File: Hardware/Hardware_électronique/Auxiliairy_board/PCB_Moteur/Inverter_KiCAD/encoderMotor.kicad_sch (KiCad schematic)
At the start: 3 parts, among them J3 Conn_02x05_Odd_Even, U1301 MAX3097ECSE+

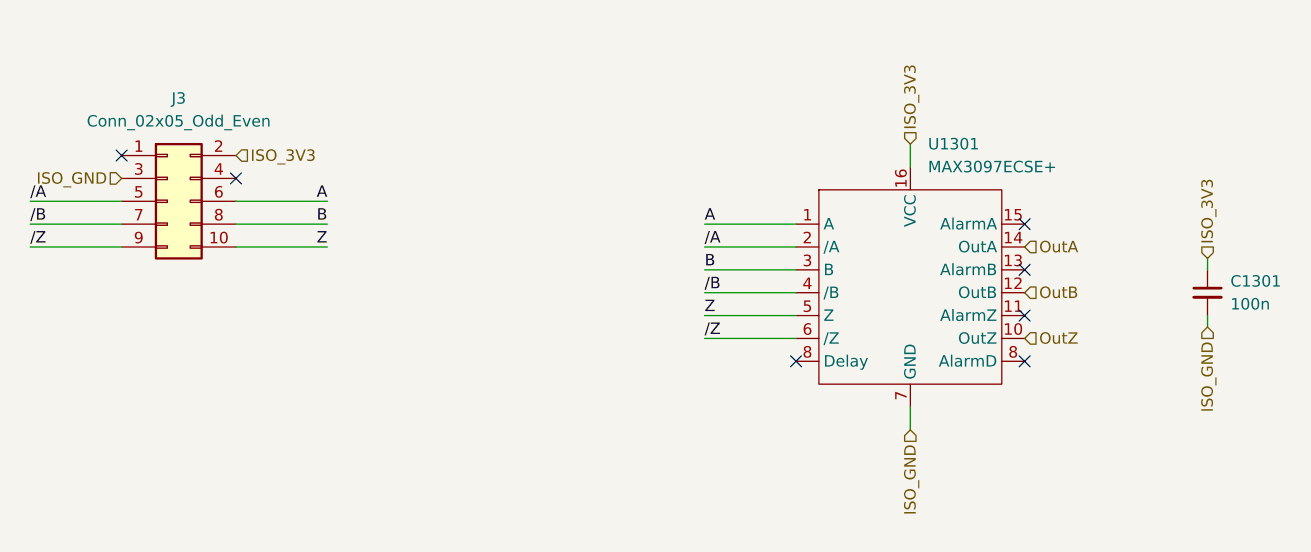
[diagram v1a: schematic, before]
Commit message: update schematic
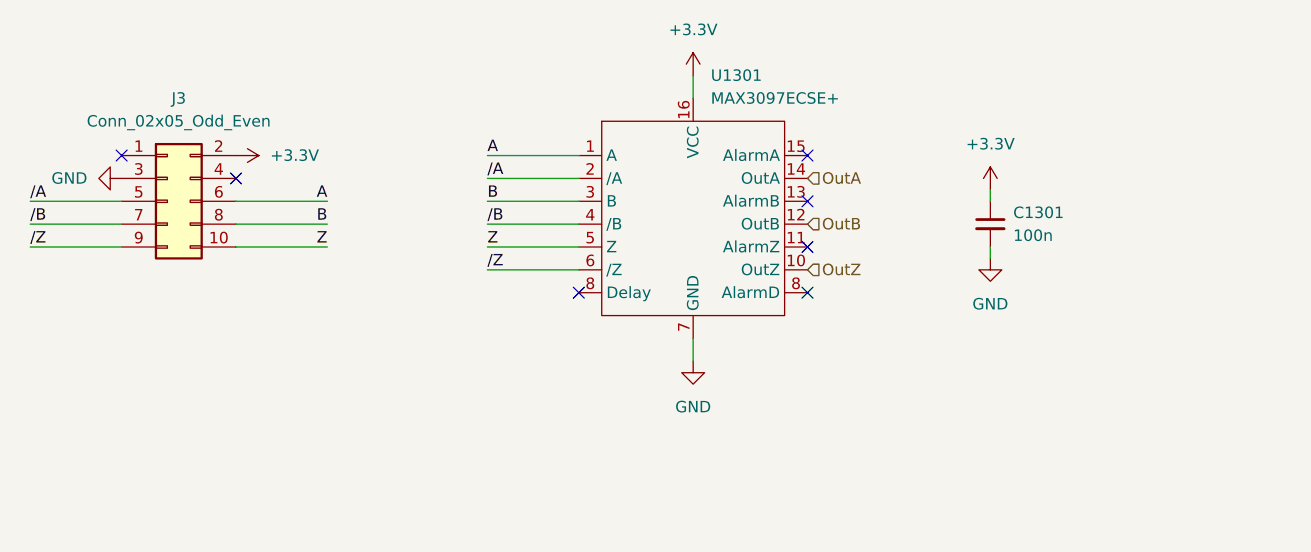
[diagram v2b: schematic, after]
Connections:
- net ISO_3V3 renamed +3.3V
- net ISO_GND renamed GND
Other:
- moved on the sheet: C1301, U1301
